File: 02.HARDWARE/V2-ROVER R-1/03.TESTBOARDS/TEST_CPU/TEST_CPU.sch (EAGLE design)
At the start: 59 parts, among them J2 302-S201, J3 DF40C-20DP-0.4V_51_, Q4 2N7002PW, Q5 2N7002PW, U1 MCP1825T-ADJE/DCSOT-223_5MC_M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, U3 ATE1D-5M3-10-Z

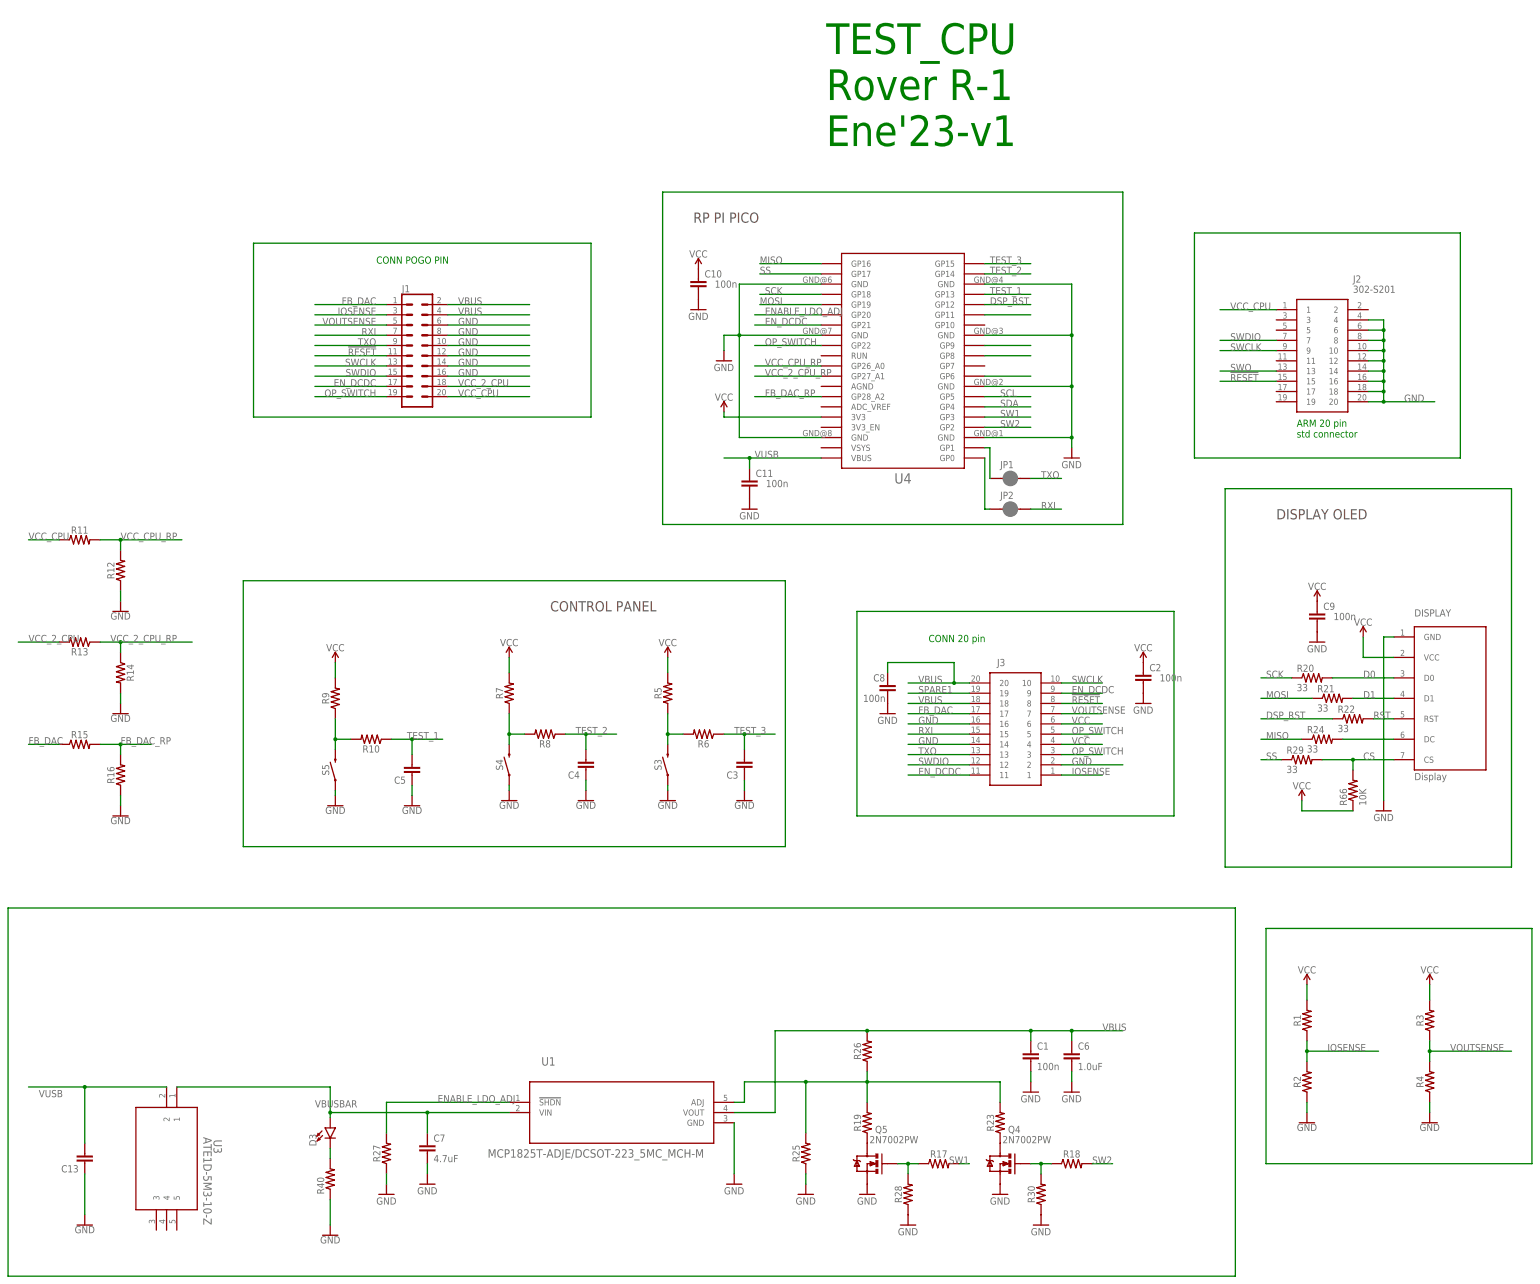
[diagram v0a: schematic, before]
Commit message: Asignacion de Valores a los componentes pasivos de las tarjetas de Testeo. Actualziacion de las BOMs.
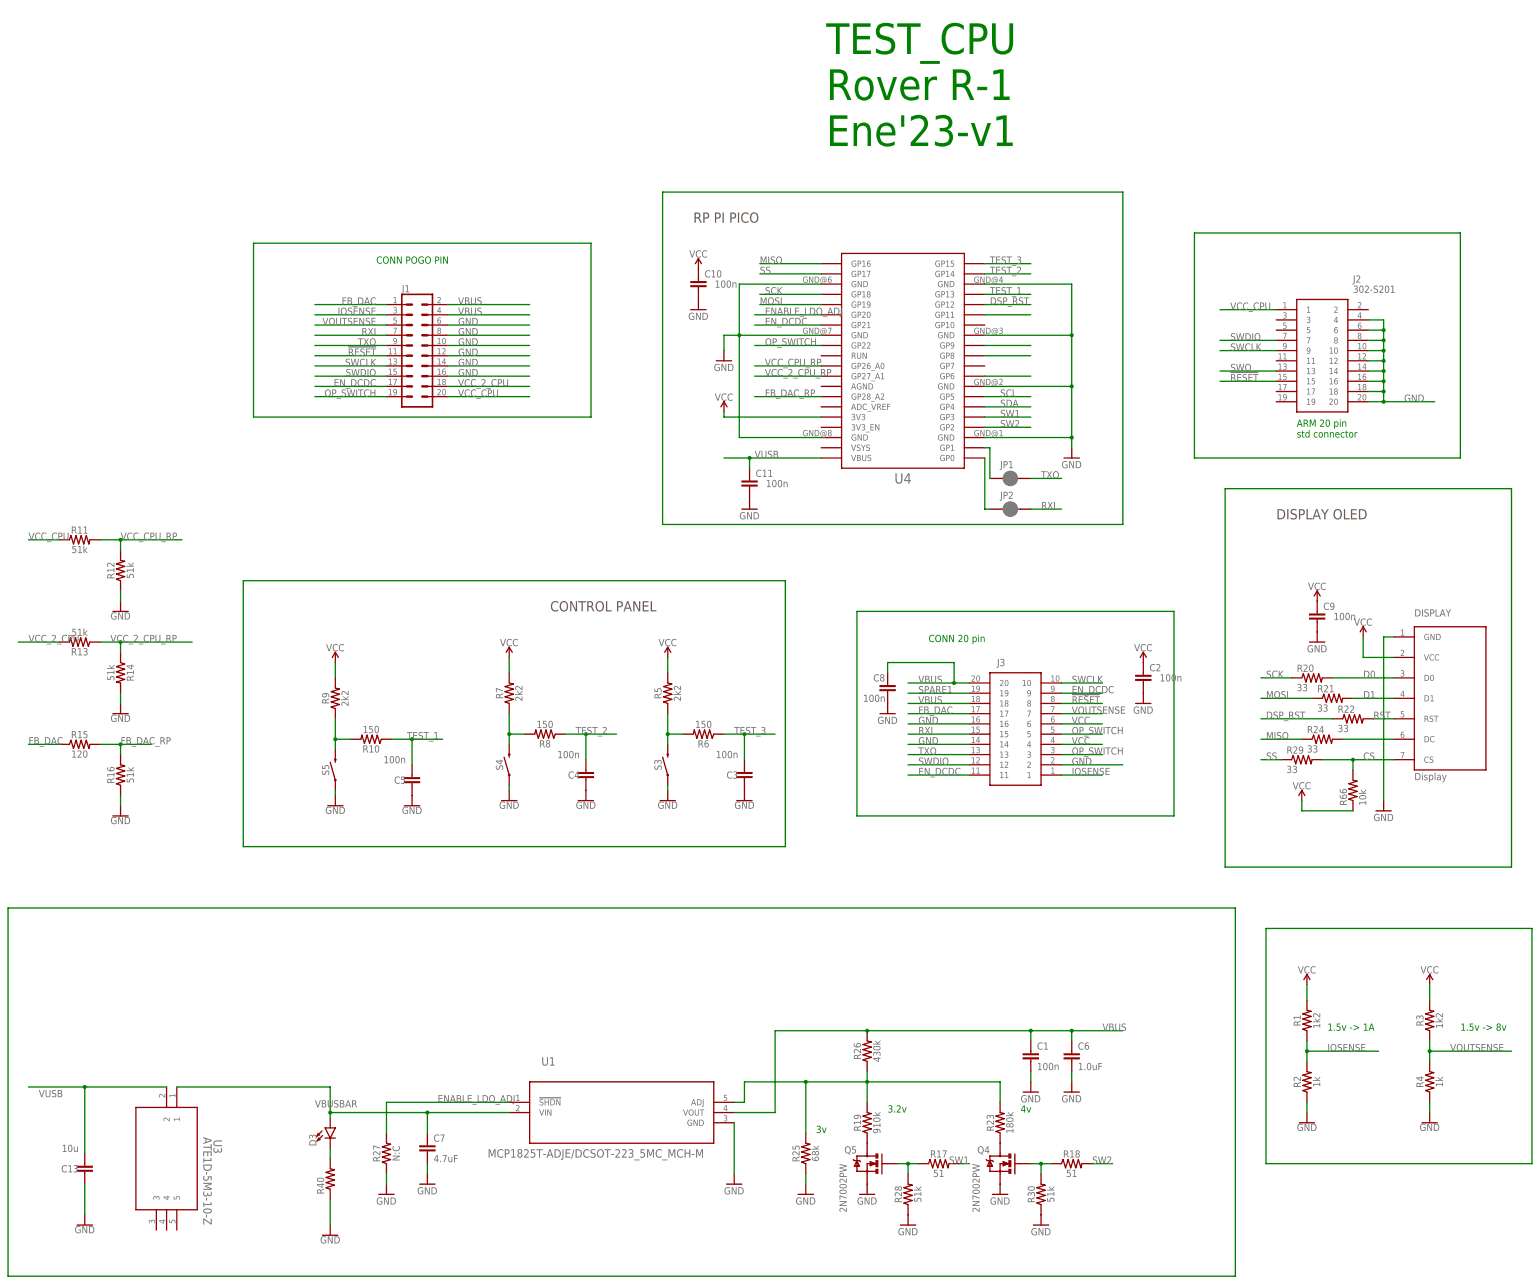
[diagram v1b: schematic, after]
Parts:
- C13: value (none) -> 10u; device rcl:C-EUC0805 -> SparkFun-Capacitors:1.0UF-0805-25V-(+80/-20%)
- C3, C4, C5: value (none) -> 100n; device rcl:C-EUC0805 -> SparkFun-Capacitors:1.0UF-0805-25V-(+80/-20%)
- C7: device SparkFun-Capacitors:4.7UF0603 -> SparkFun-Capacitors:1.0UF-0805-25V-(+80/-20%)
- R1, R3: value (none) -> 1k2
- R10, R6, R8: value (none) -> 150
- R11, R12, R13, R14, R16, R28, R30: value (none) -> 51k
- R15: value (none) -> 120
- R17, R18: value (none) -> 51
- R19: value (none) -> 910k
- R2, R4: value (none) -> 1k
- R20, R21, R22, R24, R29: device SparkFun:RESISTOR0805-RES -> SparkFun-Resistors:RESISTOR0805
- R23: value (none) -> 180k
- R25: value (none) -> 68k
- R26: value (none) -> 430k
- R27: value (none) -> N:C
- R40: value 10K -> 360; device SparkFun:RESISTOR0805-RES -> SparkFun-Resistors:RESISTOR0805
- R5, R7, R9: value (none) -> 2k2
- R66: value 10K -> 10k; device SparkFun:RESISTOR0805-RES -> SparkFun-Resistors:RESISTOR0805
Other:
- note added: "1.5v -> 1A"
- note added: "1.5v -> 8v"
- note added: "3.2v"
- note added: "3v"
- note added: "4v"
- moved on the sheet: C13, C3, C4, C5
